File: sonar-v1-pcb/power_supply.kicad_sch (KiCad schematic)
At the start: 2 parts

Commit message: Do some power work
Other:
- moved on the sheet: R138, TP78
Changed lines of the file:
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@@
 	(text_box "R = 150k * ((1.213V - (-12V)) / (1.213V) - 1)\nR = 1.48M\nClosest match is 1.47M"
 		(exclude_from_sim no)
-		(at 152.4 201.93 0)
+		(at 148.59 199.39 0)
 		(size 52.07 7.62)
 		(margins 0.9525 0.9525 0.9525 0.9525)
@@
 	)
 	(junction
-		(at 208.28 177.8)
+		(at 204.47 175.26)
 		(diameter 0)
 		(color 0 0 0 0)
@@
 	(wire
 		(pts
-			(xy 208.28 177.8) (xy 222.25 177.8)
+			(xy 204.47 175.26) (xy 218.44 175.26)
 		)
 		(stroke
@@
 	(wire
 		(pts
-			(xy 194.31 177.8) (xy 208.28 177.8)
+			(xy 190.5 175.26) (xy 204.47 175.26)
 		)
 		(stroke
@@
 	(wire
 		(pts
-			(xy 194.31 184.15) (xy 207.01 184.15)
+			(xy 190.5 181.61) (xy 203.2 181.61)
 		)
 		(stroke
@@
 	(wire
 		(pts
-			(xy 261.62 177.8) (xy 255.27 177.8)
+			(xy 257.81 175.26) (xy 251.46 175.26)
 		)
 		(stroke
@@
 	(wire
 		(pts
-			(xy 194.31 191.77) (xy 207.01 191.77)
+			(xy 190.5 189.23) (xy 203.2 189.23)
 		)
 		(stroke
@@
 	)
 	(label "-10V"
-		(at 261.62 177.8 180)
+		(at 257.81 175.26 180)
 		(effects
 			(font
@@
 	)
 	(label "-12V"
-		(at 200.66 177.8 180)
+		(at 196.85 175.26 180)
 		(effects
 			(font
@@
 	)
 	(label "-12V"
-		(at 215.9 177.8 0)
+		(at 212.09 175.26 0)
 		(effects
 			(font
@@
 	(symbol
 		(lib_id "Connector:TestPoint_Probe")
-		(at 208.28 177.8 0)
+		(at 204.47 175.26 0)
 		(unit 1)
 		(body_style 1)
@@
 		(dnp no)
 		(property "Reference" "TP78"
-			(at 209.55 170.18 0)
+			(at 205.74 167.64 0)
 			(show_name no)
 			(do_not_autoplace no)
@@
 		)
 		(property "Value" "-12V"
-			(at 209.55 172.72 0)
+			(at 205.74 170.18 0)
 			(show_name no)
 			(do_not_autoplace no)
@@
 		)
 		(property "Footprint" ""
-			(at 213.36 177.8 0)
+			(at 209.55 175.26 0)
 			(hide yes)
 			(show_name no)
@@
 		)
 		(property "Datasheet" ""
-			(at 213.36 177.8 0)
+			(at 209.55 175.26 0)
 			(hide yes)
 			(show_name no)
@@
 		)
 		(property "Description" "test point (alternative probe-style design)"
-			(at 208.28 177.8 0)
+			(at 204.47 175.26 0)
 			(hide yes)
 			(show_name no)
@@
 	(symbol
 		(lib_id "sonar_lib:R_0603_1.47M")
-		(at 207.01 187.96 0)
+		(at 203.2 185.42 0)
 		(mirror y)
 		(unit 1)
@@
 		(dnp no)
 		(property "Reference" "R138"
-			(at 204.47 186.6899 0)
+			(at 200.66 184.1499 0)
 			(show_name no)
 			(do_not_autoplace no)
@@
 		)
 		(property "Value" "1.47M"
-			(at 204.47 189.2299 0)
+			(at 200.66 186.6899 0)
 			(show_name no)
 			(do_not_autoplace no)
@@
 		)
 		(property "Footprint" "Sonar:R_0603_1608Metric"
-			(at 207.01 165.862 0)
+			(at 203.2 163.322 0)
 			(hide yes)
 			(show_name no)
@@
 		)
 		(property "Datasheet" "https://www.lcsc.com/datasheet/C166897.pdf"
-			(at 207.01 168.402 0)
+			(at 203.2 165.862 0)
 			(hide yes)
 			(show_name no)
@@
 		)
 		(property "Description" "1.47M 1% Resistor, 100mW Max Power, 75V Max Voltage, 100ppm"
-			(at 206.756 161.036 0)
+			(at 202.946 158.496 0)
 			(hide yes)
 			(show_name no)
@@
 		)
 		(property "Manufacturer" "RALEC"
-			(at 207.01 155.194 0)
+			(at 203.2 152.654 0)
 			(hide yes)
 			(show_name no)
@@
 		)
 		(property "MPN" "RTT031474FTP"
-			(at 207.01 163.322 0)
+			(at 203.2 160.782 0)
 			(hide yes)
 			(show_name no)
@@
 		)
 		(property "LCSC ID" "C166897"
-			(at 207.01 159.004 0)
+			(at 203.2 156.464 0)
 			(hide yes)
 			(show_name no)
@@
 		)
 		(property "Package" "0603"
-			(at 207.01 156.972 0)
+			(at 203.2 154.432 0)
 			(hide yes)
 			(show_name no)
@@
 	)
 	(sheet
-		(at 160.02 71.12)
+		(at 156.21 68.58)
 		(size 34.29 22.86)
 		(exclude_from_sim no)
@@
 		)
 		(property "Sheetname" "Vin to 12V Boost"
-			(at 160.02 70.4084 0)
+			(at 156.21 67.8684 0)
 			(show_name no)
 			(do_not_autoplace no)
@@
 		)
 		(property "Sheetfile" "5v_to_12v_boost.kicad_sch"
-			(at 160.02 94.5646 0)
+			(at 156.21 92.0246 0)
 			(show_name no)
 			(do_not_autoplace no)
@@
 		)
 		(pin "GND" input
-			(at 160.02 90.17 180)
+			(at 156.21 87.63 180)
 			(effects
 				(font
@@
 		)
 		(pin "Vin" input
-			(at 160.02 74.93 180)
+			(at 156.21 72.39 180)
 			(effects
 				(font
@@
 		)
 		(pin "Vout" output
-			(at 194.31 74.93 0)
+			(at 190.5 72.39 0)
 			(effects
 				(font
@@
 	)
 	(sheet
-		(at 222.25 172.72)
+		(at 218.44 170.18)
 		(size 33.02 22.86)
 		(exclude_from_sim no)
@@
 		)
 		(property "Sheetname" "-10V Negative LDO"
-			(at 222.25 172.0084 0)
+			(at 218.44 169.4684 0)
 			(show_name no)
 			(do_not_autoplace no)
@@
 		)
 		(property "Sheetfile" "-10v_negative_ldo.kicad_sch"
-			(at 222.25 196.1646 0)
+			(at 218.44 193.6246 0)
 			(show_name no)
 			(do_not_autoplace no)
@@
 		)
 		(pin "GND" input
-			(at 222.25 191.77 180)
+			(at 218.44 189.23 180)
 			(effects
 				(font
@@
 		)
 		(pin "Vin" input
-			(at 222.25 177.8 180)
+			(at 218.44 175.26 180)
 			(effects
 				(font
@@
 		)
 		(pin "Vout" output
-			(at 255.27 177.8 0)
+			(at 251.46 175.26 0)
 			(effects
 				(font
@@
 	)
 	(sheet
-		(at 160.02 172.72)
+		(at 156.21 170.18)
 		(size 34.29 22.86)
 		(exclude_from_sim no)
@@
 		)
 		(property "Sheetname" "Vin to -12V Inverting Buck Boost"
-			(at 160.02 172.0084 0)
+			(at 156.21 169.4684 0)
 			(show_name no)
 			(do_not_autoplace no)
@@
 		)
 		(property "Sheetfile" "inverting_buck_boost.kicad_sch"
-			(at 160.02 196.1646 0)
+			(at 156.21 193.6246 0)
 			(show_name no)
 			(do_not_autoplace no)
@@
 		)
 		(pin "GND" input
-			(at 160.02 191.77 180)
+			(at 156.21 189.23 180)
 			(effects
 				(font
@@
 		)
 		(pin "R_set_fb" passive
-			(at 194.31 184.15 0)
+			(at 190.5 181.61 0)
 			(effects
 				(font
@@
 		)
 		(pin "R_set_out" passive
-			(at 194.31 191.77 0)
+			(at 190.5 189.23 0)
 			(effects
 				(font
@@
 		)
 		(pin "Vin" input
-			(at 160.02 177.8 180)
+			(at 156.21 175.26 180)
 			(effects
 				(font
@@
 		)
 		(pin "Vout" output
-			(at 194.31 177.8 0)
+			(at 190.5 175.26 0)
 			(effects
 				(font
@@
 	)
 	(sheet
-		(at 160.02 135.89)
+		(at 156.21 133.35)
 		(size 34.29 22.86)
 		(exclude_from_sim no)
@@
 		)
 		(property "Sheetname" "Vin to 3.3V Buck"
-			(at 160.02 135.1784 0)
+			(at 156.21 132.6384 0)
 			(show_name no)
 			(do_not_autoplace no)
@@
 		)
 		(property "Sheetfile" "5V_in_adjustable_buck.kicad_sch"
-			(at 160.02 159.3346 0)
+			(at 156.21 156.7946 0)
 			(show_name no)
 			(do_not_autoplace no)
@@
 	)
 	(sheet
-		(at 222.25 99.06)
+		(at 218.44 96.52)
 		(size 33.02 22.86)
 		(exclude_from_sim no)
@@
 		)
 		(property "Sheetname" "12V to 10V LDO"
-			(at 222.25 98.3484 0)
+			(at 218.44 95.8084 0)
 			(show_name no)
 			(do_not_autoplace no)
@@
 		)
 		(property "Sheetfile" "12v_to_10v_ldo.kicad_sch"
-			(at 222.25 122.5046 0)
+			(at 218.44 119.9646 0)
 			(show_name no)
 			(do_not_autoplace no)
@@
 	)
 	(sheet
-		(at 222.25 135.89)
+		(at 218.44 133.35)
 		(size 33.02 22.86)
 		(exclude_from_sim no)
@@
 		)
 		(property "Sheetname" "2.75V LDO"
-			(at 222.25 135.1784 0)
+			(at 218.44 132.6384 0)
 			(show_name no)
 			(do_not_autoplace no)
@@
 		)
 		(property "Sheetfile" "2.75V_ldo.kicad_sch"
-			(at 222.25 159.3346 0)
+			(at 218.44 156.7946 0)
 			(show_name no)
 			(do_not_autoplace no)
@@
 		)
 		(pin "GND" input
-			(at 222.25 154.94 180)
+			(at 218.44 152.4 180)
 			(effects
 				(font
@@
 		)
 		(pin "Vin" input
-			(at 222.25 139.7 180)
+			(at 218.44 137.16 180)
 			(effects
 				(font
@@
 		)
 		(pin "Vout" output
-			(at 255.27 139.7 0)
-			(effects
-				(font
+			(at 251.46 137.16 0)
+			(effects
+				(font

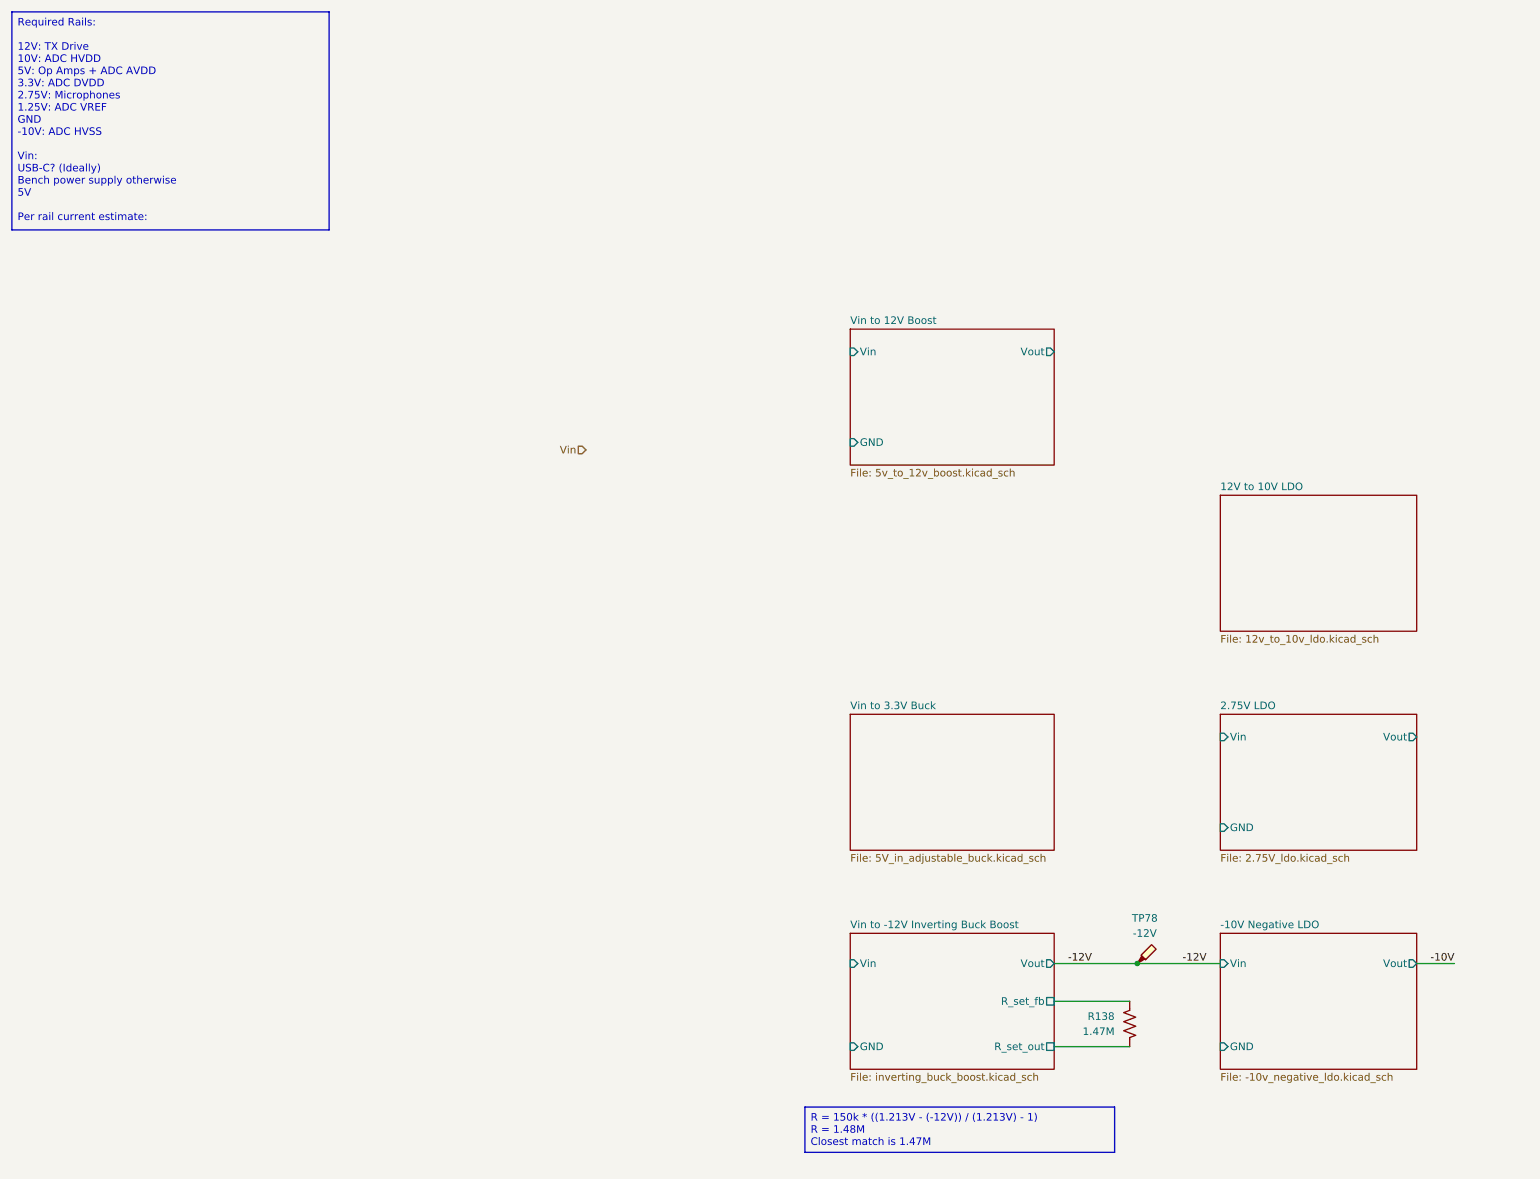
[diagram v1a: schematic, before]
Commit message: T-012: prune power tree to four rails (drop 6 legacy sheets, rewire supply/top)
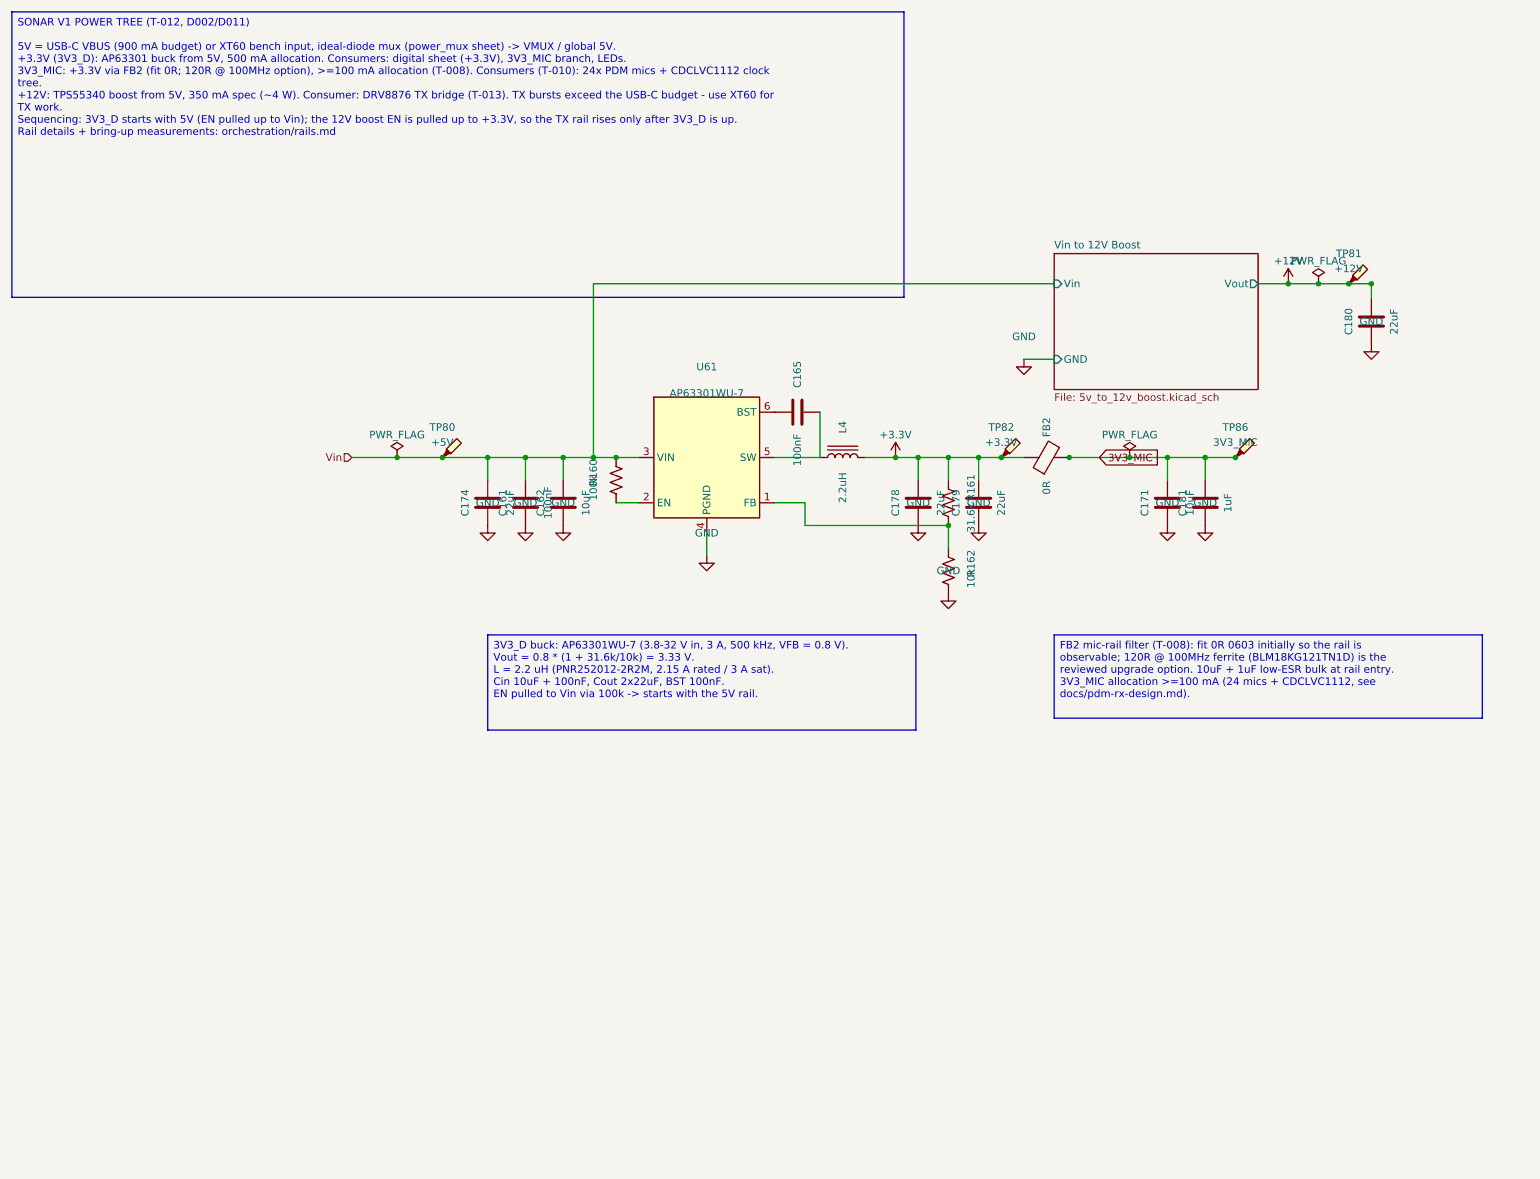
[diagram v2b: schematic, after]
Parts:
- removed R138: 1.47M, Sonar:R_0603_1608Metric, symbol sonar_lib:R_0603_1.47M
- removed TP78: -12V, symbol Connector:TestPoint_Probe
- added C161, C165: 100nF, Sonar:C_0603_1608Metric, symbol sonar_lib:C_0603_100nF
- added C162, C171: 10uF, Sonar:C_0603_1608Metric, symbol sonar_lib:C_0603_10uF
- added C174, C178, C179, C180: 22uF, Sonar:C_0603_1608Metric, symbol sonar_lib:C_0603_22uF
- added C181: 1uF, Sonar:C_0603_1608Metric, symbol sonar_lib:C_0603_1uF
- added FB2: 0R, Sonar:L_0603_1608Metric, symbol sonar_lib:FB_0603_120R
- added L4: 2.2uH, Sonar:L_1008_2520Metric, symbol sonar_lib:L_1008_2.2uH
- added R160: 100k, Sonar:R_0603_1608Metric, symbol sonar_lib:R_0603_100k
- added R161: 31.6k, Sonar:R_0603_1608Metric, symbol sonar_lib:R_0603_31.6k
- added R162: 10k, Sonar:R_0603_1608Metric, symbol sonar_lib:R_0603_10k
- added TP80: +5V, symbol Connector:TestPoint_Probe
- added TP81: +12V, symbol Connector:TestPoint_Probe
- added TP82: +3.3V, symbol Connector:TestPoint_Probe
- added TP86: 3V3_MIC, symbol Connector:TestPoint_Probe
- added U61: AP63301WU-7, Sonar:TSOT-23-6, symbol sonar_lib:AP63301WU-7
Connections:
- net Vin: now also C161.1, C162.1, C174.1, R160.1, TP80.1, U61.3 (VIN)
- new net: R161.2, R162.1, U61.1 (FB)
- new net: R160.2, U61.2 (EN)
- new net: C165.2, L4.1, U61.5 (SW)
- new net: C165.1, U61.6 (BST)
- new net +12V: C180.1, TP81.1
- new net +3.3V: C178.1, C179.1, FB2.1, L4.2, R161.1, TP82.1
- new net 3V3_MIC: C171.1, C181.1, FB2.2, TP86.1
- new net GND: C161.2, C162.2, C171.2, C174.2, C178.2, C179.2, C180.2, C181.2, R162.2, U61.4 (PGND)
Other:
- removed sheet -10V Negative LDO
- removed sheet 12V to 10V LDO
- removed sheet 2.75V LDO
- removed sheet Vin to -12V Inverting Buck Boost
- removed sheet Vin to 3.3V Buck
